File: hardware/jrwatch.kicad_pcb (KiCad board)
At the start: 4 copper layers, 36 x 36 mm, 47 parts, among them J1 TYPE-C-31-M-12, J2 FH12A-10S-0.5SH, J3 SM02B-SRSS-TB, J4 TC2030-IDC-NL, SW1 PWR/SHIP, SW2 USER, U1 MDBT50Q-1MV2, U2 nPM1300-QEAA-R7, U3 BMI270, U4 USBLC6-2SC6, Y1 32.768kHz

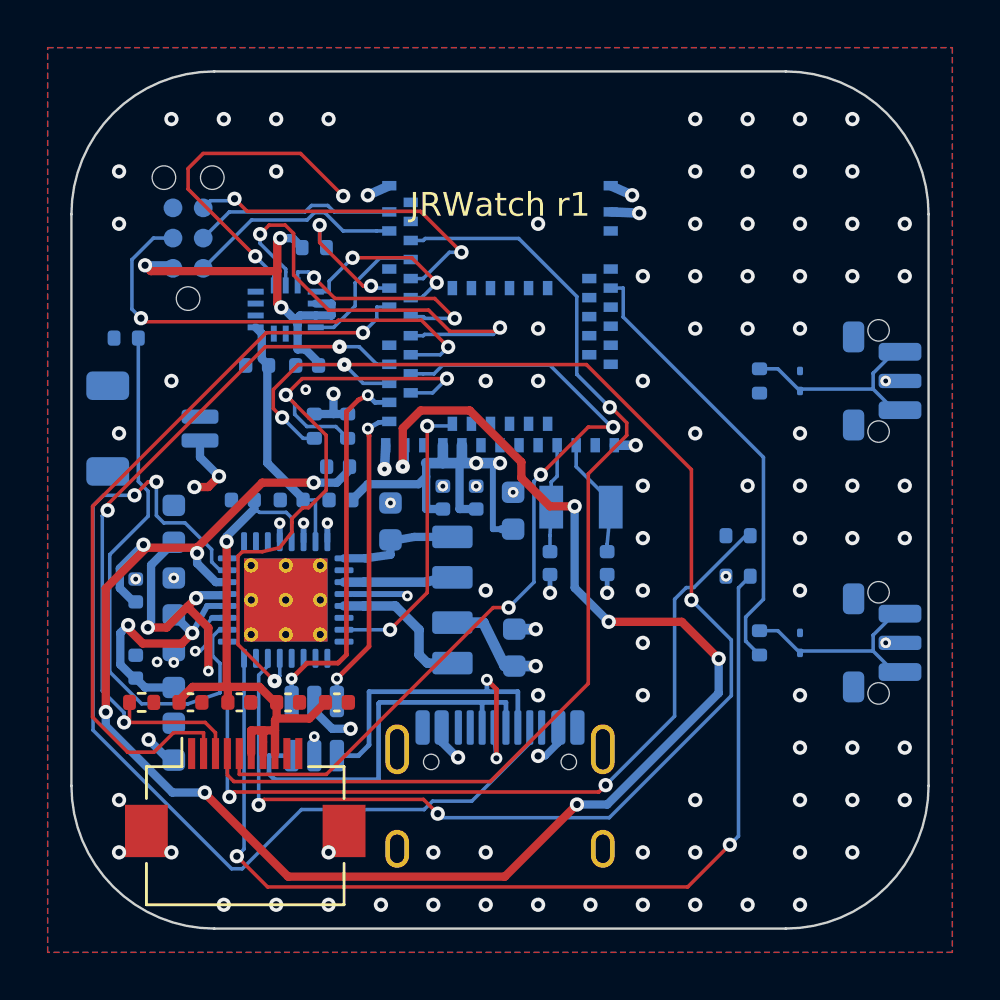
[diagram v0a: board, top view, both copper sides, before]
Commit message: D-025 WIP: land the connector, trim MP tabs, partial re-route
The position D-025 recorded as final does not work as drawn. With J2 at
(100, 107.75) the stock FH12 mounting tabs span y 108.05-110.25 and the
USB-C pad field starts at 108.83, so the two connectors occupy the same
space. DRC does not catch it because both are GND.

D-025 already called for trimming the MP pads; that is done here. The
tabs now run y 107.00-108.58, clearing J1 by 0.25 mm and keeping
2.84 mm2 of the original 3.96 mm2 anchor area by extending north into
free space instead of just cutting.

Also landed: J2 at (100, 107.75) with pad k carrying panel terminal
11-k, the GND stitch via that fell under the new pad row removed, one
GND island stitched, and DISP_ON / EXTCOMIN / VDD_DISP / DISP_MOSI plus
part of DISP_CS re-routed (Freerouting for the fabric, the A* completer
for the rest).

Still open, and the reason this stays on a branch: DISP_SCK, the rest of
DISP_CS, 3V0 pin 12, SHPHLD, CC2, and three GND zone links. Freerouting
plateaus and the A* completer cannot open a corridor for them; both
report no path. These need interactive rip-up-and-retry.

Not orderable. 8 unconnected, 20 DRC errors (8 are the pre-existing
SKRTLAE010 pad-to-NPTH geometry, 4 are J2/J1 courtyard overlap on two
hand-soldered parts).
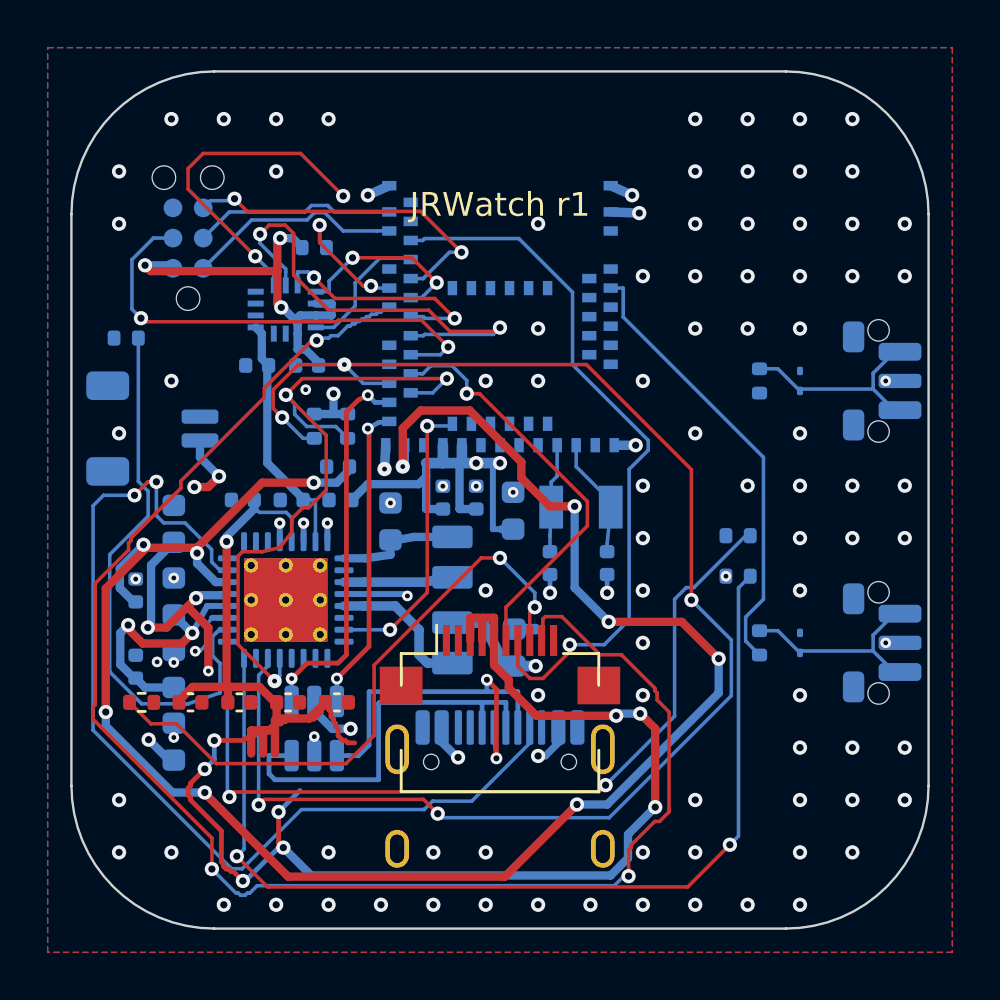
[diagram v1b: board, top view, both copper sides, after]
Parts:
- moved J2 11.7 mm to (100.0, 107.8)
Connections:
- J2 pad 1: DISP_SCK -> GND
- J2 pad 10: GND -> DISP_SCK
- J2 pad 2: DISP_MOSI -> GND
- J2 pad 3: DISP_CS -> VDD_DISP
- J2 pad 4: EXTCOMIN -> VDD_DISP
- J2 pad 5: DISP_ON -> VDD_DISP
- J2 pad 6: VDD_DISP -> DISP_ON
- J2 pad 7: VDD_DISP -> EXTCOMIN
- J2 pad 8: VDD_DISP -> DISP_CS
- J2 pad 9: GND -> DISP_MOSI
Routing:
- net VDD_DISP: track 23.9 -> 78.6 mm, vias 1 -> 9
- net DISP_MOSI: track 31.6 -> 66.1 mm, vias 1 -> 3
- net DISP_ON: track 34.8 -> 17.5 mm, vias 3 -> 1
- net EXTCOMIN: track 43.7 -> 30.3 mm
- net DISP_CS: track 30.2 -> 26.1 mm, vias 3 -> 2
